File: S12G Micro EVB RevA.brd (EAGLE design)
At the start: 49 x 21 mm, 35 parts, among them IC1 FT232RL, IC2 MCP1640, J2 JUMPER

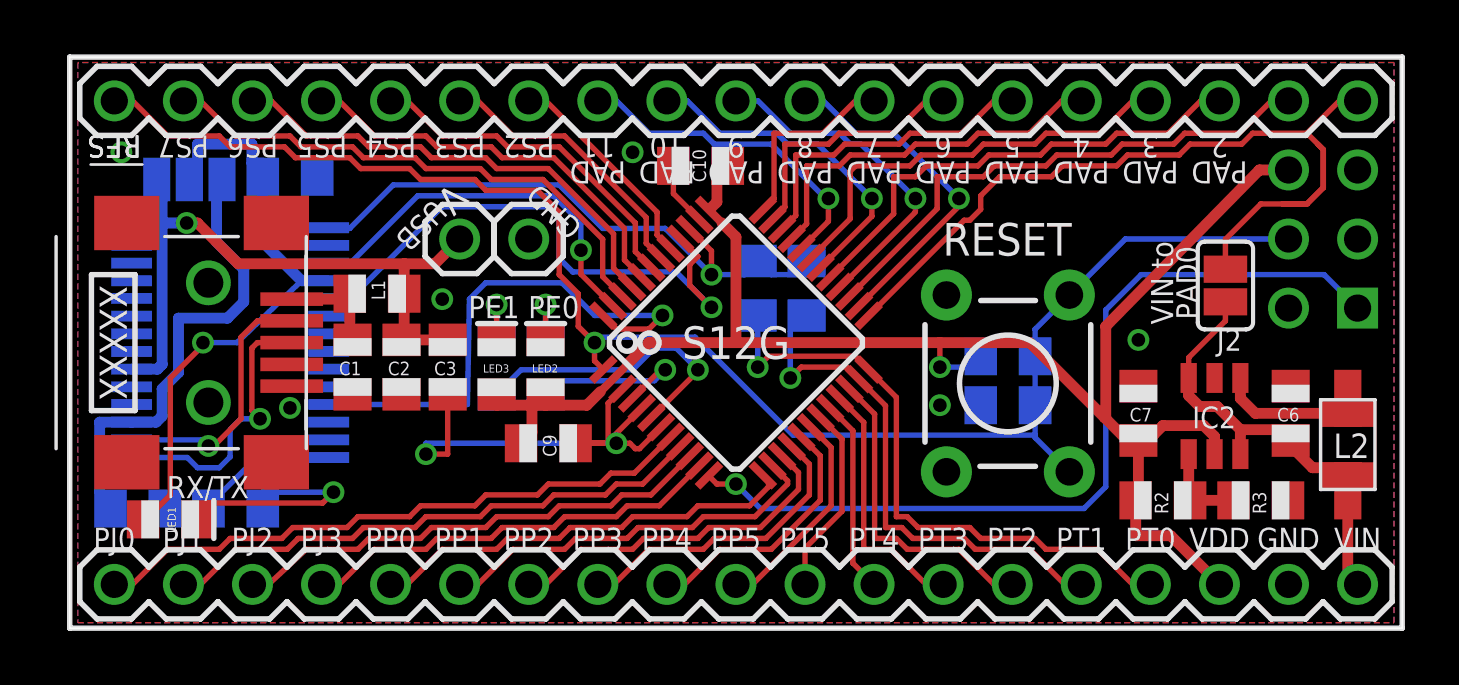
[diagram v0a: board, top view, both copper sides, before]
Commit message: added BOM
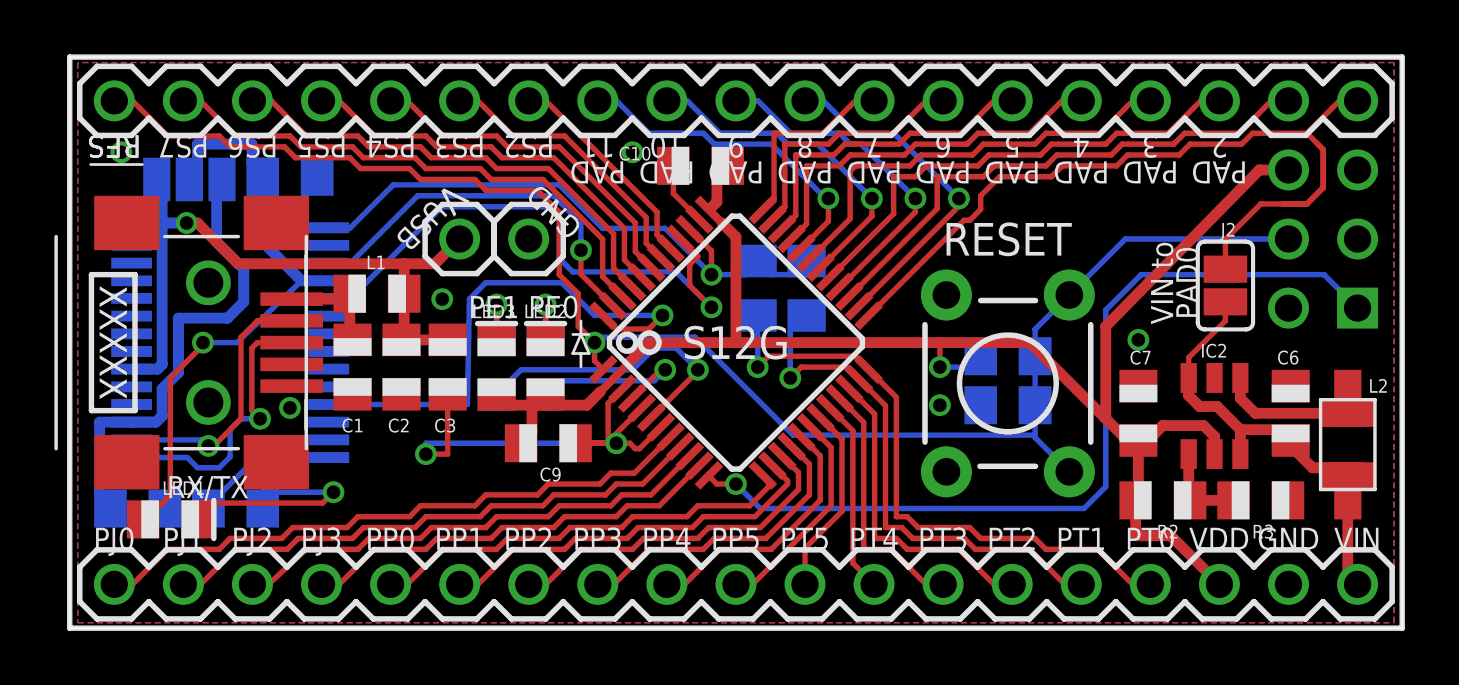
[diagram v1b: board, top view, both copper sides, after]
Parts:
- R1, R7, R8: value 270 -> 120
- R2: value 976K -> 820K
- R3: value 563K -> 470K
- R5, R6: value 270 -> 330
